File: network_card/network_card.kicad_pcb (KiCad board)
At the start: 2 copper layers, 100 x 92 mm, 27 parts, among them IC1 SN74HCT138N, IC2 SN74HCT138N, J1 Conn1, J2 INT_EN, J3 SPI_Header, U1 74HC04, U10 74LS08, U2 74HCT163E, U3 74LS32, U4 74LS08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

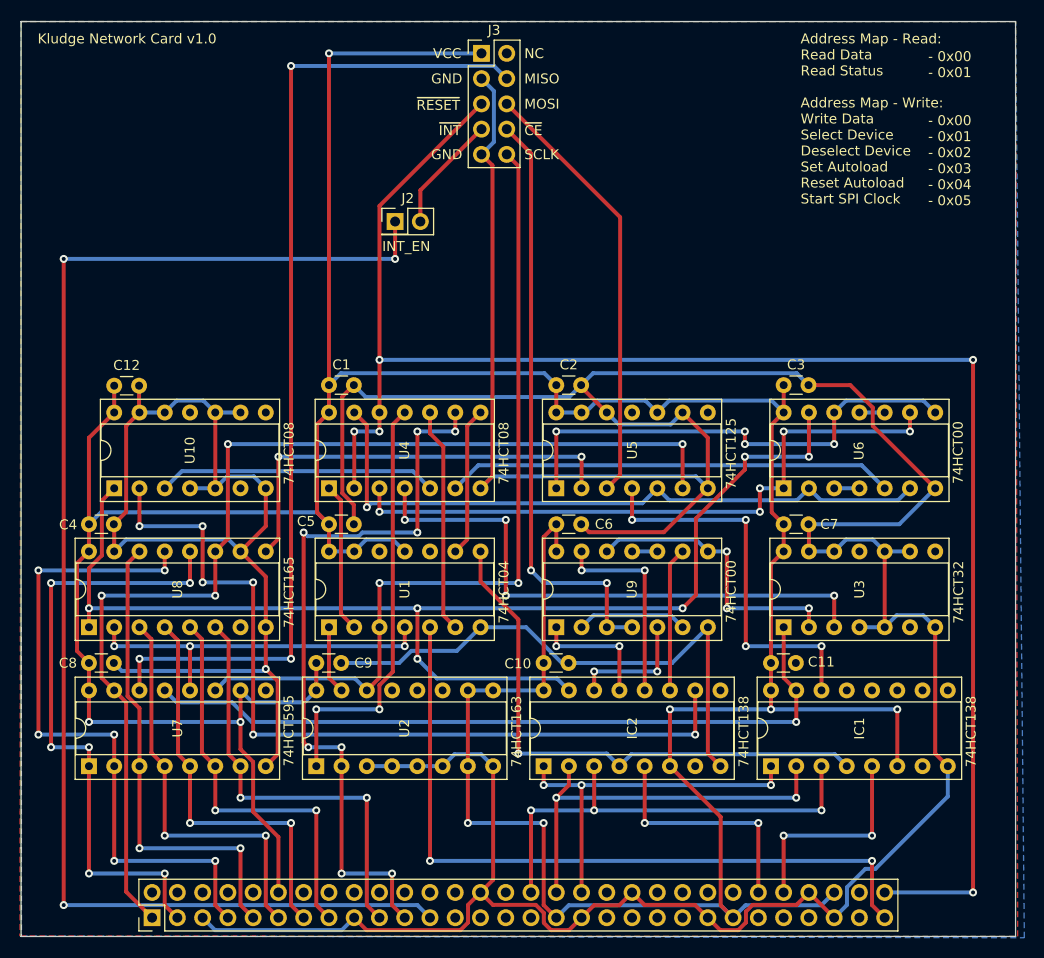
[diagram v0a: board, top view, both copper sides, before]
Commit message: Fixed misplacement of network module footprint. Added second footprint on edge of PCB for IDC connector
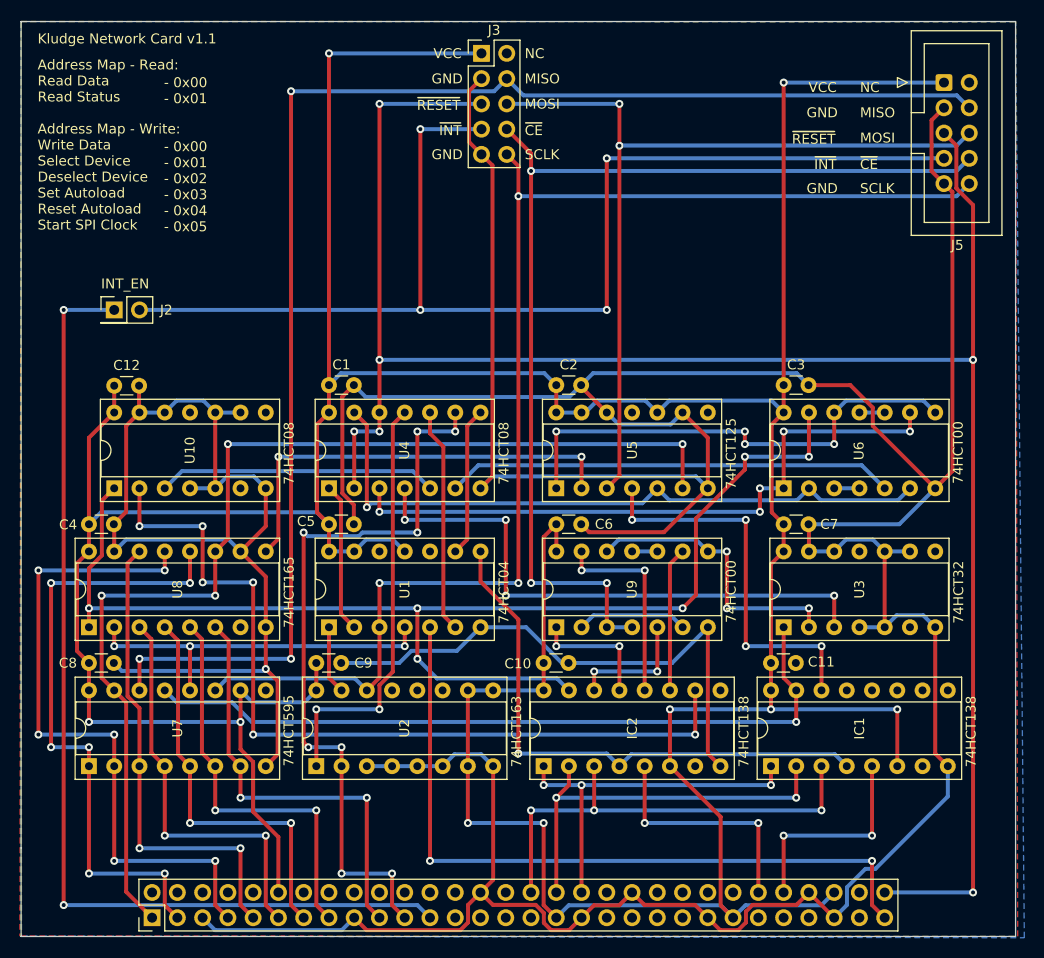
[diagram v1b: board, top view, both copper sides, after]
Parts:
- added J5: SPI_Header, Connector_IDC:IDC-Header_2x05_P2.54mm_Vertical, F.Cu at (190.0, 62.4)
- moved J2 29.6 mm to (106.6, 85.2)
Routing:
- net Net-(J2-Pin_2): track 11.8 -> 120.5 mm, vias 0 -> 4
- net VCC: track 410.9 -> 457.4 mm, vias 8 -> 9
- net SPI_CLK: track 85.2 -> 131.0 mm, vias 2 -> 3
- net ~{SPI_CS}: track 60.5 -> 105.8 mm, vias 2 -> 3
- net MISO: track 100.2 -> 145.4 mm
- net MOSI: track 43.9 -> 86.2 mm, vias 0 -> 2
- net GND: track 527.8 -> 568.2 mm
- net ~{INT}: track 139.4 -> 102.3 mm, vias 3 -> 2
- net ~{RESET}: track 167.6 -> 197.6 mm, vias 5 -> 6
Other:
- board text added: "Kludge Network Card v1.1"
- board text removed: "Kludge Network Card v1.0"
